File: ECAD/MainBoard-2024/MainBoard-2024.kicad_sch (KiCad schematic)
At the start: 65 parts, among them J1 XT60, J10 Conn_01x02, J11 Conn_01x03, J12 Conn_01x04, J13 Conn_01x03, J14 Conn_01x03, J15 Conn_01x02, J16 XT30, J17 XT30, J18 Conn_01x02, J2 Conn_01x04, J20 BAU, J21 BAU, J22 Conn_01x04, J23 Conn_01x02, J26 BAU, J27 BAU, J28 Conn_01x02, J29 Conn_01x02, J3 ConStep1, J4 Conn_01x02, J5 ConStep1, J6 ConStep1, J7 XT30, J8 Conn_01x02, J9 Conn_01x02, K2 FINDER-36.11, U1 Teensy3.5_All_Pins, U2 R-78B3.3-2.0, U3 R-78B12-2.0, U4 R-78B5.0-2.0

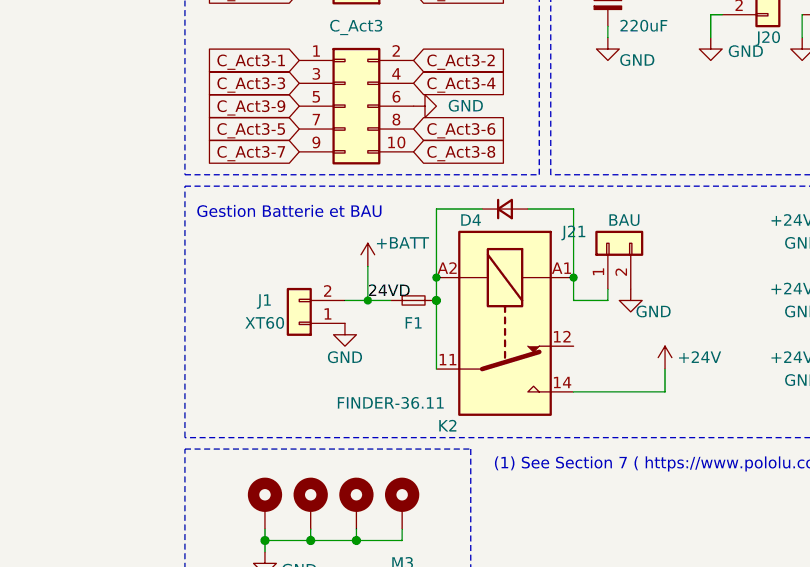
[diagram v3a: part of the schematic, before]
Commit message: Power trace routing
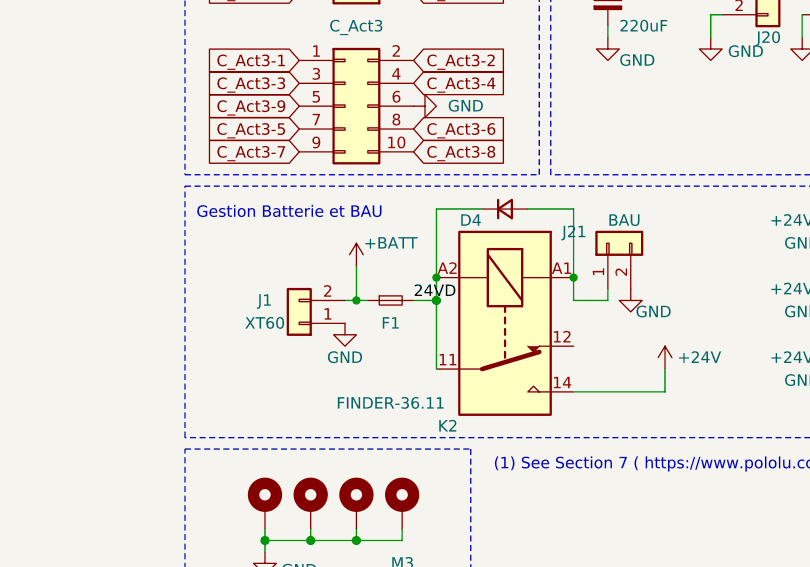
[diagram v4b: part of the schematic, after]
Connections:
- net 24VD: now reaches D4.1 (K), F1.2, K2.11, K2.A2
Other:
- moved on the sheet: F1
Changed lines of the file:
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@@
   (junction (at 203.2 57.15) (diameter 1.016) (color 0 0 0 0)
   )
+  (junction (at 162.56 149.86) (diameter 0) (color 0 0 0 0)
+  )
   (junction (at 207.01 27.94) (diameter 0) (color 0 0 0 0)
   )
@@
   (junction (at 171.45 149.86) (diameter 1.016) (color 0 0 0 0)
   )
-  (junction (at 163.83 149.86) (diameter 0) (color 0 0 0 0)
-  )
   (junction (at 162.56 176.53) (diameter 1.016) (color 0 0 0 0)
   )
@@
     (stroke (width 0) (type solid))
   )
-  (wire (pts (xy 163.83 149.86) (xy 166.37 149.86))
+  (wire (pts (xy 162.56 149.86) (xy 163.83 149.86))
     (stroke (width 0) (type default))
   )
@@
     (stroke (width 0) (type solid))
   )
-  (wire (pts (xy 163.83 146.05) (xy 163.83 149.86))
+  (wire (pts (xy 162.56 146.05) (xy 162.56 149.86))
     (stroke (width 0) (type default))
   )
@@
     (stroke (width 0) (type dash))
   )
+  (wire (pts (xy 168.91 149.86) (xy 171.45 149.86))
+    (stroke (width 0) (type default))
+  )
   (wire (pts (xy 152.4 27.94) (xy 152.4 29.21))
     (stroke (width 0) (type default))
@@
     (stroke (width 0) (type solid))
   )
-  (wire (pts (xy 161.29 149.86) (xy 163.83 149.86))
+  (wire (pts (xy 161.29 149.86) (xy 162.56 149.86))
     (stroke (width 0) (type default))
   )
@@
     (effects (font (size 1.27 1.27)) (justify left bottom))
   )
-  (label "24VD" (at 163.83 149.86 0) (fields_autoplaced)
+  (label "24VD" (at 168.91 149.86 0) (fields_autoplaced)
     (effects (font (size 1.27 1.27)) (justify left bottom))
   )
@@
     )
   )
-  (symbol (lib_id "Device:Fuse_Small") (at 168.91 149.86 0) (unit 1)
+  (symbol (lib_id "Device:Fuse_Small") (at 166.37 149.86 0) (unit 1)
     (in_bom yes) (on_board yes) (dnp no) (fields_autoplaced)
-    (property "Reference" "F1" (at 168.91 152.4 0)
+    (property "Reference" "F1" (at 166.37 152.4 0)
       (effects (font (size 1.27 1.27)))
     )
-    (property "Value" "Fuse_Small" (at 167.1182 151.7401 0)
+    (property "Value" "Fuse_Small" (at 164.5782 151.7401 0)
       (effects (font (size 1.27 1.27)) hide)
     )
-    (property "Footprint" "Fuse:Fuseholder_Blade_Mini_Keystone_3568" (at 168.91 149.86 0)
+    (property "Footprint" "Fuse:Fuseholder_Blade_Mini_Keystone_3568" (at 166.37 149.86 0)
       (effects (font (size 1.27 1.27)) hide)
     )
-    (property "Datasheet" "~" (at 168.91 149.86 0)
+    (property "Datasheet" "~" (at 166.37 149.86 0)
       (effects (font (size 1.27 1.27)) hide)
     )
@@
     )
   )
-  (symbol (lib_id "power:+BATT") (at 163.83 146.05 0) (unit 1)
+  (symbol (lib_id "power:+BATT") (at 162.56 146.05 0) (unit 1)
     (in_bom yes) (on_board yes) (dnp no)
-    (property "Reference" "#PWR0141" (at 163.83 149.86 0)
+    (property "Reference" "#PWR0141" (at 162.56 149.86 0)
       (effects (font (size 1.27 1.27)) hide)
     )
-    (property "Value" "+BATT" (at 167.64 143.51 0)
+    (property "Value" "+BATT" (at 166.37 143.51 0)
       (effects (font (size 1.27 1.27)))
     )
-    (property "Footprint" "" (at 163.83 146.05 0)
+    (property "Footprint" "" (at 162.56 146.05 0)
       (effects (font (size 1.27 1.27)) hide)
     )
-    (property "Datasheet" "" (at 163.83 146.05 0)
+    (property "Datasheet" "" (at 162.56 146.05 0)
       (effects (font (size 1.27 1.27)) hide)
     )

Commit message: fix recom 78b05 orientation
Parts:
- U2, U3, U4: footprint Converter_DCDC:Converter_DCDC_RECOM_R-78E-0.5_THT -> Converter_DCDC:Converter_DCDC_RECOM_R-78B-2.0_THT
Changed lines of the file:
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@@
       (effects (font (size 1.27 1.27)))
     )
-    (property "Footprint" "Converter_DCDC:Converter_DCDC_RECOM_R-78E-0.5_THT" (at 189.23 34.29 0)
+    (property "Footprint" "Converter_DCDC:Converter_DCDC_RECOM_R-78B-2.0_THT" (at 189.23 34.29 0)
       (effects (font (size 1.27 1.27) italic) (justify left) hide)
     )
@@
       (effects (font (size 1.27 1.27)))
     )
-    (property "Footprint" "Converter_DCDC:Converter_DCDC_RECOM_R-78E-0.5_THT" (at 161.29 34.29 0)
+    (property "Footprint" "Converter_DCDC:Converter_DCDC_RECOM_R-78B-2.0_THT" (at 161.29 34.29 0)
       (effects (font (size 1.27 1.27) italic) (justify left) hide)
     )
@@
       (effects (font (size 1.27 1.27)))
     )
-    (property "Footprint" "Converter_DCDC:Converter_DCDC_RECOM_R-78E-0.5_THT" (at 215.9 34.29 0)
+    (property "Footprint" "Converter_DCDC:Converter_DCDC_RECOM_R-78B-2.0_THT" (at 215.9 34.29 0)
       (effects (font (size 1.27 1.27) italic) (justify left) hide)
     )

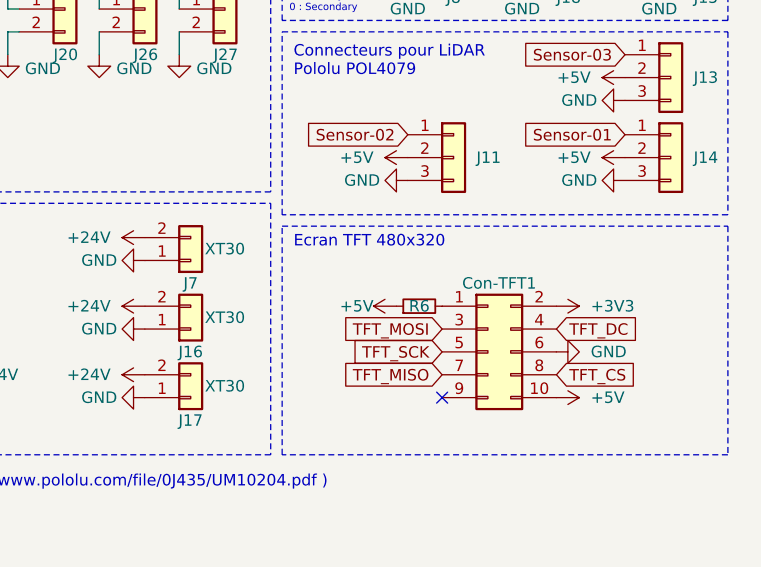
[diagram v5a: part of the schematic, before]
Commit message: change resistor value
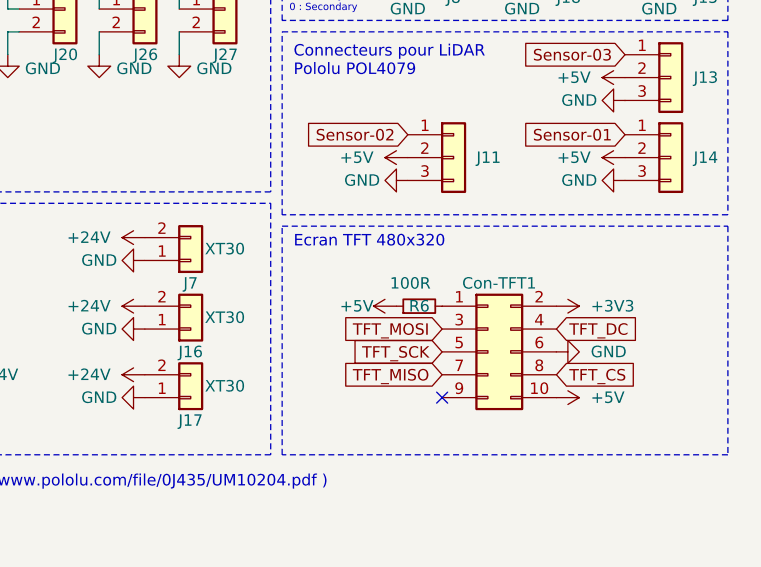
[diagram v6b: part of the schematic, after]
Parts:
- R6: value R_Small -> 100R
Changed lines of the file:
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@@
       (effects (font (size 1.27 1.27)))
     )
-    (property "Value" "R_Small" (at 249.5166 147.0913 0)
-      (effects (font (size 1.27 1.27)) (justify left) hide)
+    (property "Value" "100R" (at 248.92 146.05 90)
+      (effects (font (size 1.27 1.27)) (justify left))
     )
     (property "Footprint" "Resistor_SMD:R_1206_3216Metric_Pad1.30x1.75mm_HandSolder" (at 247.65 148.59 0)
